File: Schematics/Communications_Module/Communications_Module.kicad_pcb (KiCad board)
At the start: 4 copper layers, 69.5 x 60 mm, 72 parts, among them J1 USB_B_Micro, J2 SWD_01x04_Pin, J3 Stack Male Edge Connector, Q1 AO3400A, SW1 SW_STM_RESET, SW2 SW_STM_BOOT_MODE, U1 RFM95W-915S2, U2 W25Q128JVS, U3 AMS1117-3.3, U4 LM66100DCKR, U5 LM66100DCKR, U6 LM66100DCKR, U7 STM32F103CBT6, U8 ACS70331EOLC, U9 ISO1042BDWVR, Y1 X322516MMB4SI

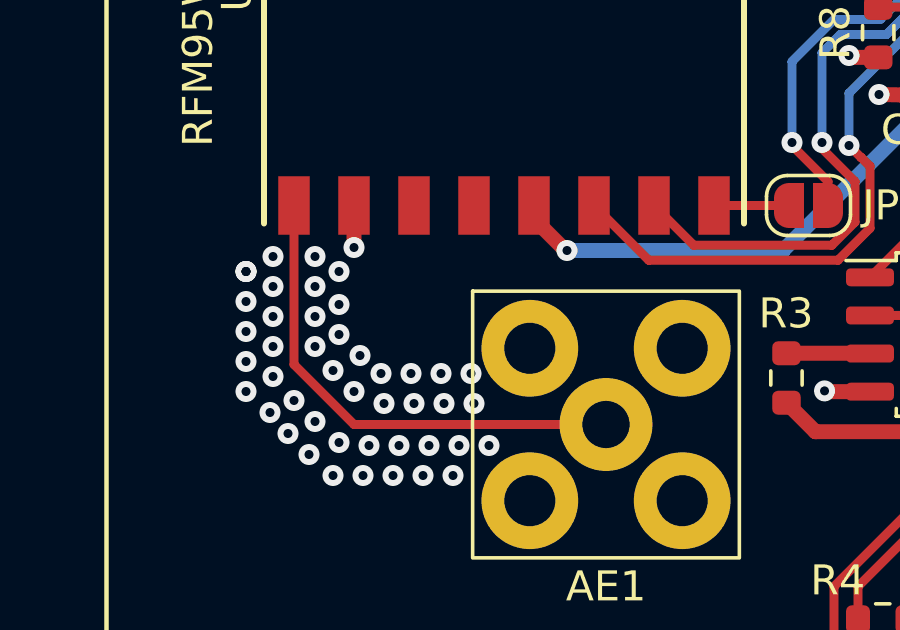
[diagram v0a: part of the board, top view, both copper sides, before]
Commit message: 50 ohm characterstic impedance antenna trace?:
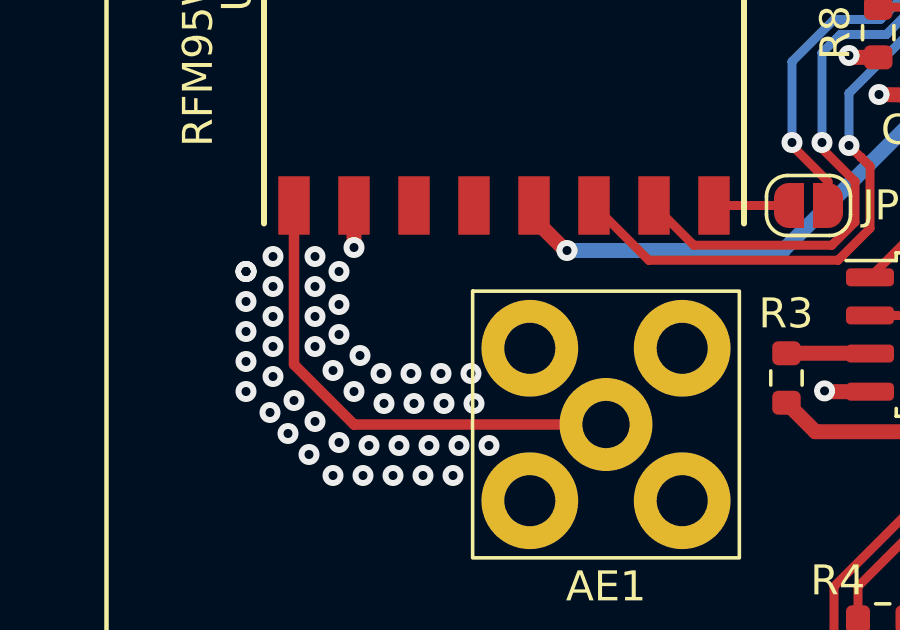
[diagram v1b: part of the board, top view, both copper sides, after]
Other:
- board text added: "Gross Trace Tracker (they all are, but here's the worst): - STM Reset - USB Diff Pair? - SCK_FL - Curr_sense - MOSI_RF - RF DIOx traces - Buzzer (PWM right? something should prob be done about that one) - Can_Rx/Tx traces? - batt_sense mightve forgot more"
- board text added: "need to confirm this trace -50 ohm characteristic impedance? via fence can block up to like 20 GHz"
- board text removed: "Gross Trace Tracker (they all are, but here's the worst): - STM Reset - USB Diff Pair? - SCK_FL - Curr_sense - MOSI_RF - RF DIOx traces - Buzzer (PWM right? something should prob be done about that one) - Can_Rx/Tx traces? - batt_sense"
- board text removed: "need to confirm this trace via fence can block up to like 20 GHz"
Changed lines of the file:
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@@
     (effects (font (size 1 1) (thickness 0.15)) (justify left bottom))
   )
-  (gr_text "need to confirm this trace\nvia fence can block up to like 20 GHz" (at 73.8 124.2) (layer "Cmts.User")
+  (gr_text "need to confirm this trace \n-50 ohm characteristic impedance?\nvia fence can block up to like 20 GHz" (at 73.8 124.2) (layer "Cmts.User")
     (effects (font (size 1 1) (thickness 0.15)) (justify left bottom))
   )
@@
     (effects (font (size 1 1) (thickness 0.15)) (justify left bottom))
   )
-  (gr_text "Gross Trace Tracker (they all are, but here's the worst):\n- STM Reset\n- USB Diff Pair?\n- SCK_FL\n- Curr_sense\n- MOSI_RF\n- RF DIOx traces\n- Buzzer (PWM right? something should prob be done about that one)\n- Can_Rx/Tx traces?\n- batt_sense" (at 112.75 160.25) (layer "Cmts.User")
+  (gr_text "Gross Trace Tracker (they all are, but here's the worst):\n- STM Reset\n- USB Diff Pair?\n- SCK_FL\n- Curr_sense\n- MOSI_RF\n- RF DIOx traces\n- Buzzer (PWM right? something should prob be done about that one)\n- Can_Rx/Tx traces?\n- batt_sense\nmightve forgot more" (at 112.75 160.25) (layer "Cmts.User")
     (effects (font (size 1 1) (thickness 0.15)) (justify left bottom))
   )
@@
   (segment (start 133.5 78.2) (end 133.5 84.141947) (width 0.3) (layer "F.Cu") (net 17))
   (segment (start 132.68 89.235) (end 133.5 89.235) (width 0.3) (layer "F.Cu") (net 17))
-  (segment (start 116.5 115.9) (end 116.5 121.2) (width 0.3) (layer "F.Cu") (net 22))
-  (segment (start 118.5 123.2) (end 126.9 123.2) (width 0.3) (layer "F.Cu") (net 22))
-  (segment (start 116.5 121.2) (end 118.5 123.2) (width 0.3) (layer "F.Cu") (net 22))
+  (segment (start 116.5 115.9) (end 116.5 121.2) (width 0.3493) (layer "F.Cu") (net 22))
+  (segment (start 118.5 123.2) (end 126.9 123.2) (width 0.3493) (layer "F.Cu") (net 22))
+  (segment (start 116.5 121.2) (end 118.5 123.2) (width 0.3493) (layer "F.Cu") (net 22))
   (segment (start 126.075 91.2) (end 125.08 91.2) (width 0.5) (layer "F.Cu") (net 23))
   (segment (start 125.08 91.2) (end 123.3 89.42) (width 0.5) (layer "F.Cu") (net 23))

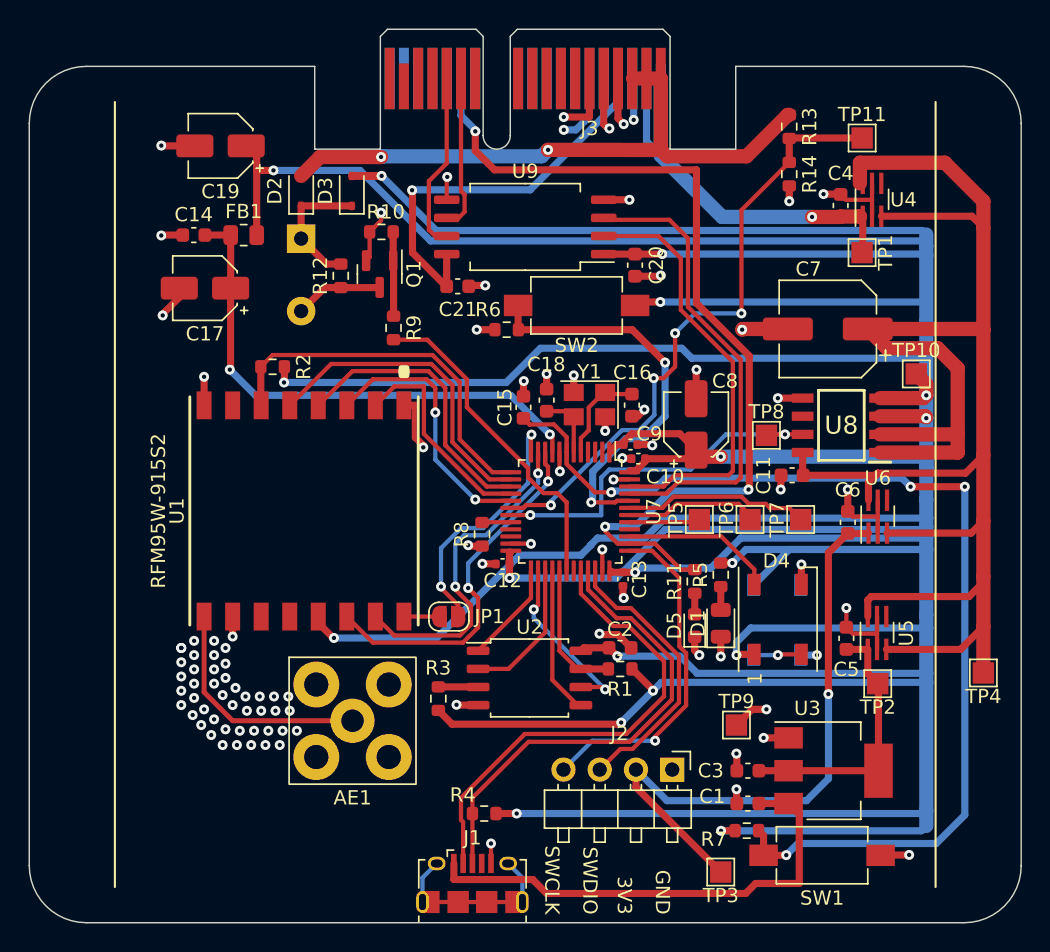
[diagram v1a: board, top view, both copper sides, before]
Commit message: Layout updated accordingly, DRC mostly done (some silk screen overlap)
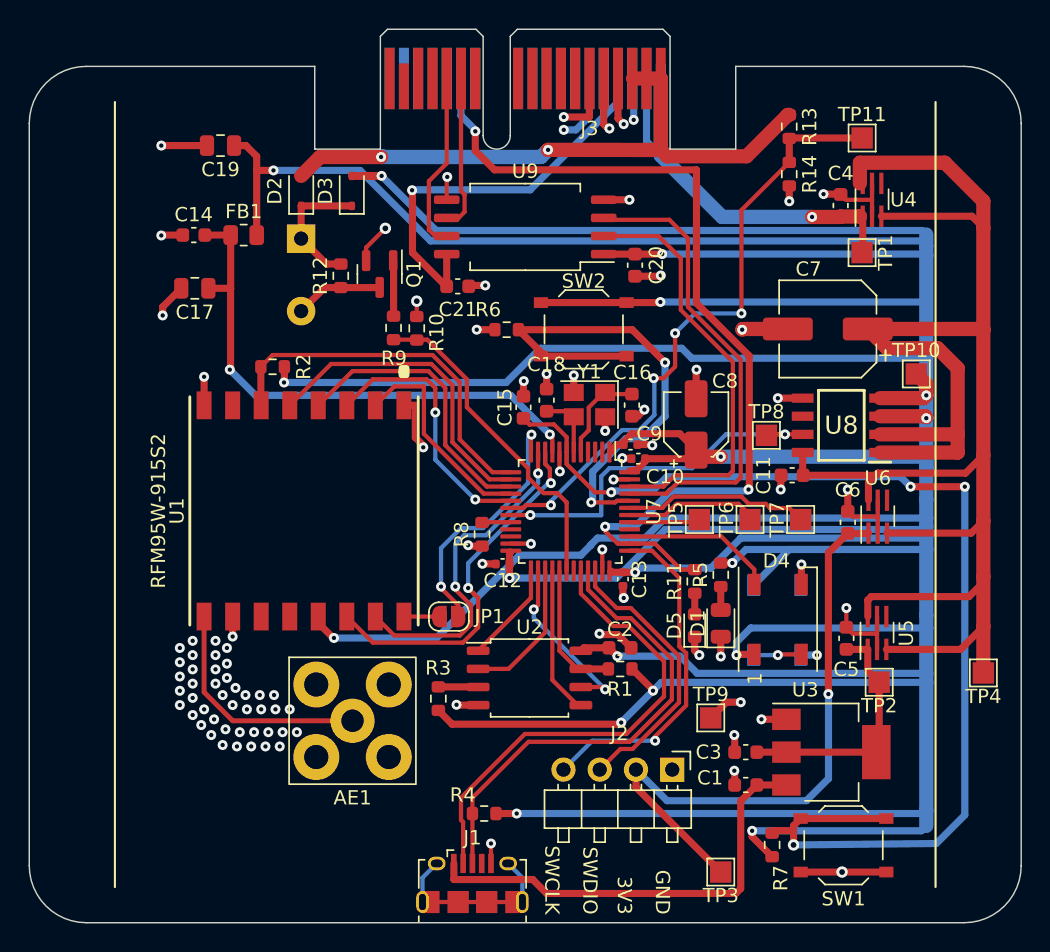
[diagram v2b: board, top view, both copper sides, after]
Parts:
- C17, C19: footprint Capacitor_SMD:CP_Elec_4x5.4 -> Capacitor_SMD:C_0805_2012Metric
- SW1, SW2: footprint PTS636:PTS636_SK43_SMTR_LFS -> Button_Switch_SMD:SW_Push_1P1T_XKB_TS-1187A
- moved R10 7.19 mm to (131.4, 95.7), turned to -90 degrees
- moved R7 2.04 mm to (156.3, 131.9), turned to -90 degrees
- moved TP9 1.87 mm to (152.0, 123.0)
- moved SW2 1.75 mm to (143.1, 95.8), turned to 180 degrees
- moved SW1 1.66 mm to (161.3, 131.9)
- moved C1 1.31 mm to (154.4, 127.7)
- moved C3 1.31 mm to (154.4, 125.4)
- moved U3 1.31 mm to (160.4, 125.4)
- moved C17 0.71 mm to (115.8, 92.9)
- moved TP2 0.14 mm to (163.8, 120.5)
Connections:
- net V_BATT renamed +BATT
- J3 pad A13: DB_LED -> unconnected-(J3-DB_LED-PadA13)
- R10 pad 2: Net-(Q1-G) -> BUZZER
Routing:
- net BOOT0: track 28.3 -> 35.0 mm
- net +3.3V: track 526.1 -> 531.8 mm
- net STM_RESET: track 75.0 -> 80.5 mm
- net GND: track 108.7 -> 113.5 mm, vias 96 -> 95
- net /USB_5V: track 34.0 -> 31.6 mm
- net Net-(Q1-G): track 5.91 -> 3.90 mm
- net +3.3VA: track 37.1 -> 38.6 mm
- net V_REGUSB: track 18.7 -> 17.6 mm
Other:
- board text added: "worried about noise (especially from buzzer) on analogue trace - Buzzer PWM trace runs near a lot of other traces"
- board text removed: "worried about noise (especially from buzzer) on analogue trace"

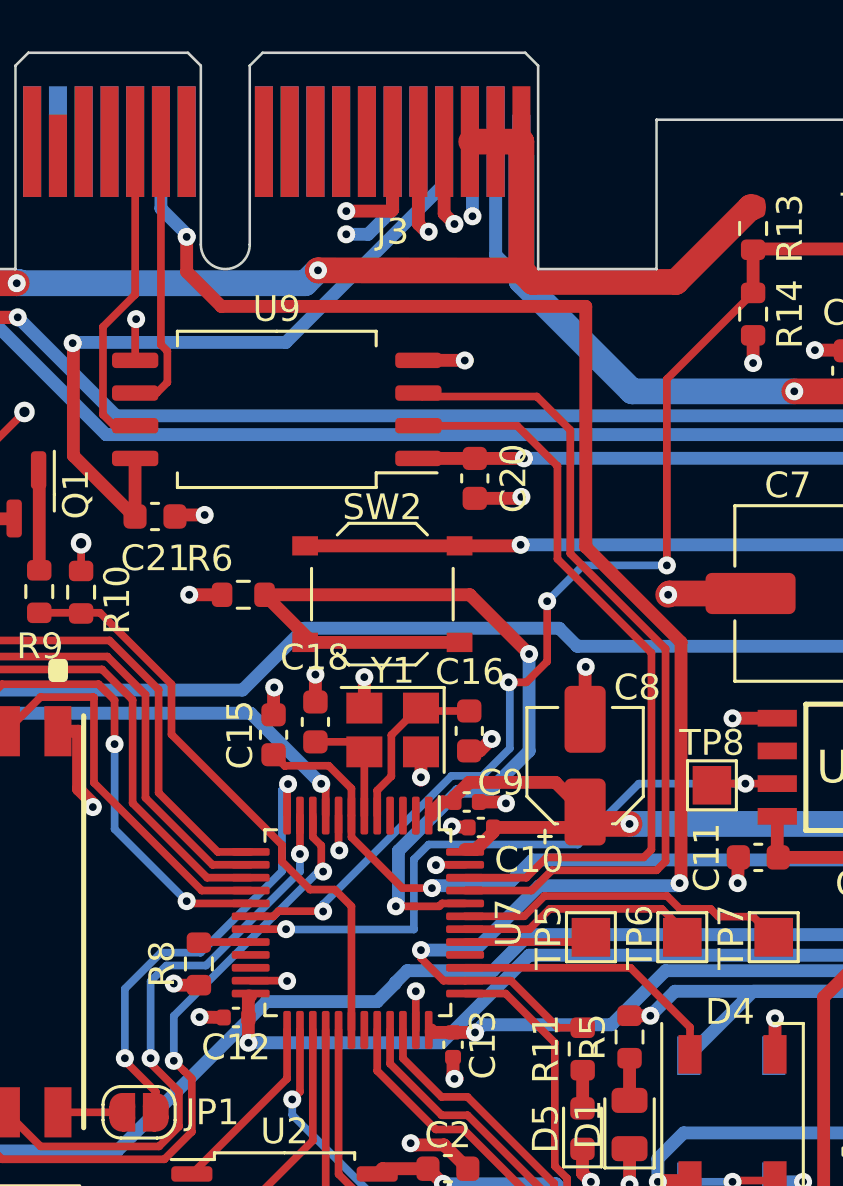
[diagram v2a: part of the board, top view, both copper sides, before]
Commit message: Removed DB_LED trace from edge connector
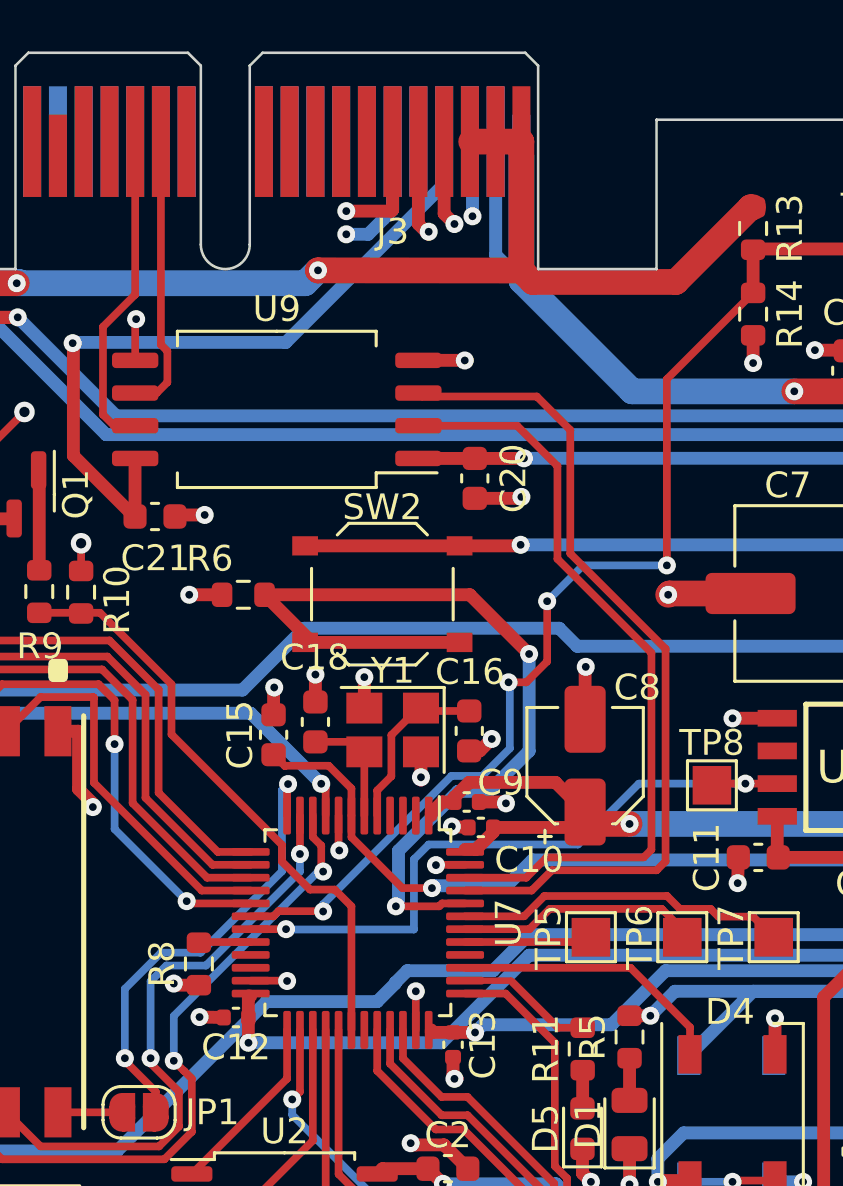
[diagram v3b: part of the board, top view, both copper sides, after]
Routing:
- net DB_LED: track 64.6 -> 5.32 mm, vias 3 -> 0
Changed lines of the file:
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@@
   (segment (start 140.6 83.2) (end 140.1 83.7) (width 1) (layer "B.Cu") (net 4))
   (segment (start 140.1 83.7) (end 128.9 83.7) (width 1) (layer "B.Cu") (net 4))
-  (segment (start 144.6 109.913541) (end 144.6 109.6) (width 0.3) (layer "F.Cu") (net 9))
-  (segment (start 148.094606 110.7875) (end 149.922106 112.615) (width 0.3) (layer "F.Cu") (net 9))
-  (segment (start 154.7 97.643502) (end 151 93.943502) (width 0.5) (layer "F.Cu") (net 9))
-  (segment (start 151 84.6) (end 136.846472 84.6) (width 0.5) (layer "F.Cu") (net 9))
-  (segment (start 154.645309 106.99904) (end 154.7 106.944349) (width 0.5) (layer "F.Cu") (net 9))
+  (segment (start 146.3125 110.7875) (end 148.094606 110.7875) (width 0.25) (layer "F.Cu") (net 9))
   (segment (start 149.922106 112.615) (end 150.88 112.615) (width 0.3) (layer "F.Cu") (net 9))
-  (segment (start 136.846472 84.6) (end 135.5 83.253528) (width 0.5) (layer "F.Cu") (net 9))
-  (segment (start 146.3125 110.7875) (end 145.473959 110.7875) (width 0.3) (layer "F.Cu") (net 9))
-  (segment (start 145.473959 110.7875) (end 144.6 109.913541) (width 0.3) (layer "F.Cu") (net 9))
-  (segment (start 151 93.943502) (end 151 84.6) (width 0.5) (layer "F.Cu") (net 9))
-  (segment (start 135.5 83.253528) (end 135.5 81.9) (width 0.5) (layer "F.Cu") (net 9))
-  (segment (start 146.3125 110.7875) (end 148.094606 110.7875) (width 0.3) (layer "F.Cu") (net 9))
-  (segment (start 154.7 106.944349) (end 154.7 97.643502) (width 0.5) (layer "F.Cu") (net 9))
-  (segment (start 154.645309 106.99904) (end 154.677661 107.031392) (width 0.5) (layer "F.Cu") (net 9))
-  (via (at 154.645309 106.99904) (size 0.7) (drill 0.3) (layers "F.Cu" "B.Cu") (net 9))
-  (via (at 135.5 81.9) (size 0.7) (drill 0.3) (layers "F.Cu" "B.Cu") (net 9))
-  (via (at 144.6 109.6) (size 0.7) (drill 0.3) (layers "F.Cu" "B.Cu") (net 9))
-  (segment (start 135.5 81.9) (end 135.6 81.9) (width 0.5) (layer "B.Cu") (net 9))
-  (segment (start 134.5 78.2) (end 134.5 80.8) (width 0.5) (layer "B.Cu") (net 9))
-  (segment (start 134.5 80.8) (end 135.5 81.8) (width 0.5) (layer "B.Cu") (net 9))
-  (segment (start 154.645309 106.99904) (end 154.544349 107.1) (width 0.5) (layer "B.Cu") (net 9))
-  (segment (start 146.7 109.6) (end 144.6 109.6) (width 0.5) (layer "B.Cu") (net 9))
-  (segment (start 135.6 81.9) (end 135.5 81.8) (width 0.5) (layer "B.Cu") (net 9))
-  (segment (start 154.544349 107.1) (end 149.2 107.1) (width 0.5) (layer "B.Cu") (net 9))
-  (segment (start 135.5 81.8) (end 135.5 81.9) (width 0.5) (layer "B.Cu") (net 9))
-  (segment (start 149.2 107.1) (end 146.7 109.6) (width 0.5) (layer "B.Cu") (net 9))
+  (segment (start 148.153553 110.846447) (end 149.922106 112.615) (width 0.3) (layer "F.Cu") (net 9))
+  (segment (start 148.094606 110.7875) (end 148.153553 110.846447) (width 0.25) (layer "F.Cu") (net 9))
   (segment (start 134.5 86.087893) (end 134.75 86.337893) (width 0.3) (layer "F.Cu") (net 16))
   (segment (start 134.5 78.2) (end 134.5 86.087893) (width 0.3) (layer "F.Cu") (net 16))

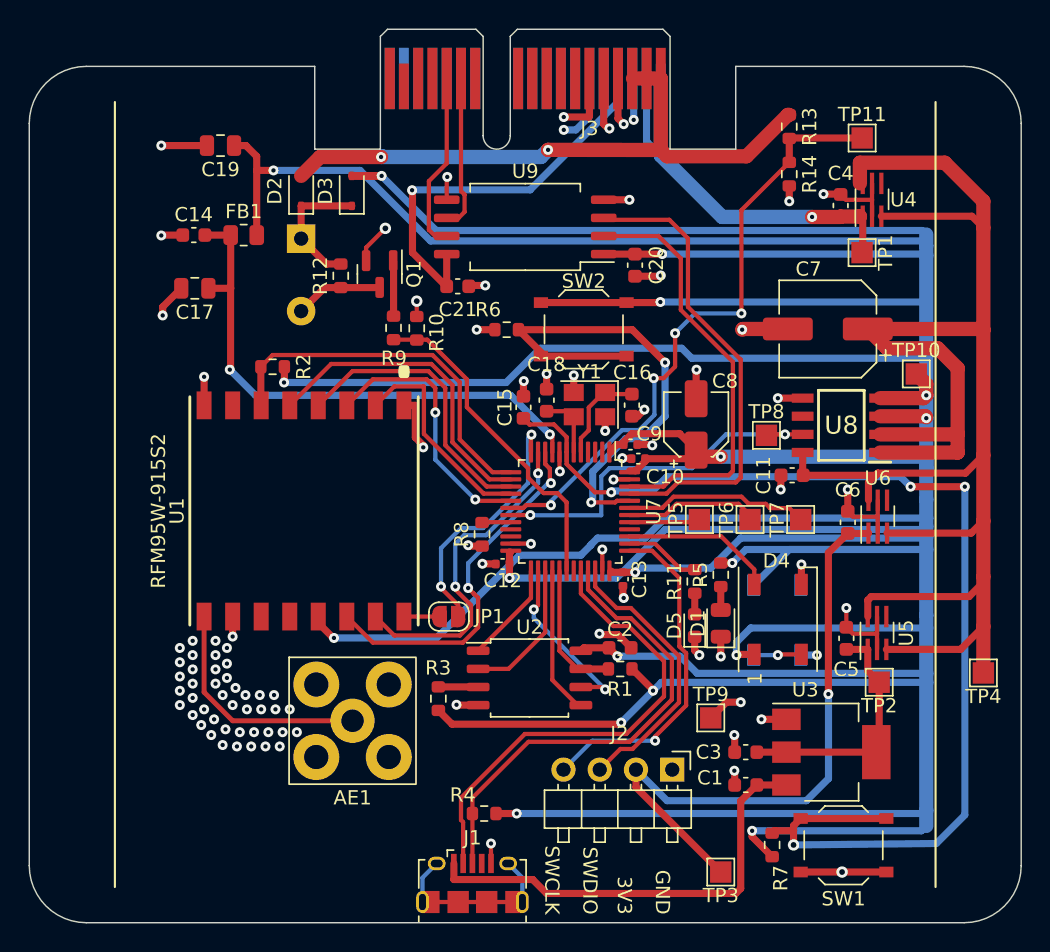
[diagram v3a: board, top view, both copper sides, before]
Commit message: All DRC passed, fixed silkscreen issues
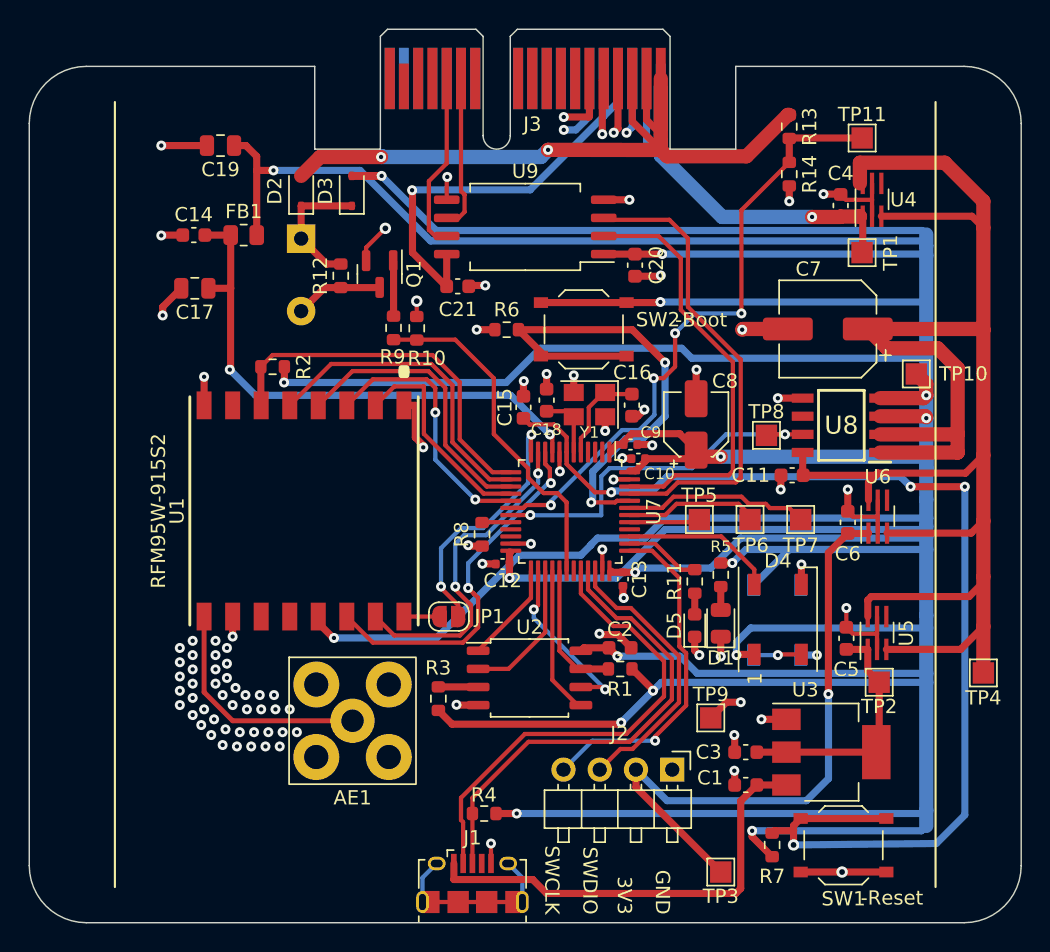
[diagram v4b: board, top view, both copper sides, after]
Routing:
- net +BATT: track 43.4 -> 51.6 mm
- net GND: track 113.5 -> 115.0 mm
- net BUZZER: track 23.2 -> 24.3 mm
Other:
- board text added: "-Boot"
- board text added: "-Reset"
